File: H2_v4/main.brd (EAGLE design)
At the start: 160 x 100 mm, 15 parts, among them Q3 SOT-23, Q4 SOT-23, Q5 SOT-23, Q6 SOT-23

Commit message: Daily updates. Schematic done, board mostly done
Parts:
- removed Q1, Q2: (no value), Custom_old (1):POWERDI3333-8
- added C1, C11, C2, C3, C5: 0.1uF, SparkFun-Passives:0603-CAP
- added C10, C12, C4, C6, C7, C8, C9: 10uF, SparkFun-Passives:1206
- added D3: (no value), SparkFun-DiscreteSemi:SOD-123
- added IC1: (no value), 2018:V78W
- added LED1, LED2: (no value), SparkFun-LED:LED-1206
- added Q7, Q8: MOSFET-NCHANNELDFN5X6, 2018:DFN5X6
- added R1, R16, R17, R2: 1k, SparkFun-Passives:0603-RES
- added R10, R11, R12, R13, R14, R9: 4.7k, SparkFun-Passives:0603-RES
- added R15, R7: 10k, SparkFun-Passives:0603-RES
- added R3, R6: open, SparkFun-Passives:0603-RES
- added R4: 200m, SparkFun-Passives:0603-RES
- added R5: 0, SparkFun-Passives:0603-RES
- added R8: 1.2k, SparkFun-Passives:0603-RES
- added U$10, U$11: PAD, Custom_old (1):PAD
- added U$12: (no value), 2018:CAP-RADIAL
- added U$13: HEADER2, Custom_old:2PINVALULOK
- added U$14, U$15, U$18, U$19: SCREW, Custom_old:M3HOLE
- added U$16, U$17: (no value), 2018:DO-214AB
- added U$20, U$9: HEADER4VALULOK, Custom_old:4PINVALULOK
- added U$8: TEENSY_3.0_BASIC, Teensy3.0:TEENSY_3.0_BASIC
- U$1: value PRO-MINI-2 -> SHUNT_KELVIN; device Arduino-clone:PRO-MINI-2 -> 2018:2512_KELVIN
- U$5: value PAD -> HEADER8; device Custom_old (1):PAD -> Custom_old:8PINVALULOK
- U$6: value PAD -> LTC7001; device Custom_old (1):PAD -> 2018:PSOP-10
- moved Q6 126.0 mm to (41.0, 58.0)
- moved Q5 124.9 mm to (49.0, 58.0)
- moved D1 120.6 mm to (36.0, 65.0), turned to 180 degrees
- moved D2 119.6 mm to (31.0, 65.0), turned to 180 degrees
- moved Q3 73.5 mm to (45.0, 58.0)
- moved U$5 72.9 mm to (23.0, 70.0)
- moved U$2 65.4 mm to (17.9, 26.7), turned to 270 degrees
- moved Q4 53.6 mm to (21.0, 57.0)
- moved U$7 53.1 mm to (47.0, 48.0)
- moved U$6 51.6 mm to (26.0, 18.0)
- moved U$4 49.1 mm to (6.00, 4.00)
- moved U$1 36.4 mm to (14.0, 9.00)
- moved U$3 36.0 mm to (6.00, 11.0)
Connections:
- removed net 12V: D1.C, D2.C, U$5.PAD, U$7.POS
- removed net BUZZER: Q5.1
- removed net N$4: Q6.3
- removed net PASS_GATE: Q2.G
- removed net SC_GATE: Q1.G
- new net 5V: C3.2, C8.1, C9.1, IC1.OUT, R5.2, U$6.1, U$8.VIN
- new net ACC: C10.1, C4.1, D1.C, D2.C, R6.2, U$20.1, U$5.6, U$5.8, U$7.POS
- new net BUTTON: R15.1, U$13.2, U$8.16/A2
- new net BUZZ_G: Q5.1, U$8.9
- new net CAP_OUT: C5.2, Q8.1, Q8.2, Q8.3, U$10.PAD, U$12.+, U$17.C, U$6.8
- new net FAN_H: D3.C, R3.1, R5.1, R6.1, U$5.4
- new net FAN_L: D3.A, Q6.3, U$5.3
- new net FAN_SENSE: C2.1, R7.2, U$8.14/A0
- new net FC_POS: C6.1, C7.1, IC1.IN, Q7.PAD, Q8.PAD, R3.2, U$1.I+
- new net FC_RAW: C12.1, U$1.I-, U$16.C, U$3.PAD
- new net LED1: R16.1, U$8.10
- new net LED2: R17.1, U$8.11
- new net N$10: R10.2, U$9.2
- new net N$11: LED2.A, R17.2
- new net N$7: R1.1, U$1.V-
- new net N$8: R2.1, U$1.V+
- new net N$9: Q6.2, R4.2, R7.1
- new net PASS_CTRL: U$6.4, U$8.7
- new net PASS_G: Q8.4, U$6.6, U$6.7
- new net RX_FLOW: R10.1, R9.1, U$8.0
- new net SCL_EXT: R12.2, U$20.4, U$8.22/A8
- new net SC_G: Q7.4, U$8.8
- new net SDA_EXT: R11.2, U$20.3, U$8.23/A9
- new net THERM: R8.2, U$5.2, U$8.15/A1
- new net TX_FLOW: U$8.1, U$9.3
- new net VBAT: U$8.VBAT
- net 3.3V: now also C11.1, R11.1, R12.1, R13.1, R14.1, R15.2, R8.1, U$8.3.3V, U$8.3.3V1
- net FAN_G: now also U$8.4
- net GND: now also C10.2, C11.2, C12.2, C2.2, C3.1, C4.2, C6.2, C7.2, C8.2, C9.2, IC1.GND, LED1.C, LED2.C, Q7.1, Q7.2, Q7.3, R4.1, R9.2, U$11.PAD, U$12.-, U$13.1, U$16.A, U$17.A, U$20.2, U$4.PAD, U$5.1, U$6.2, U$6.3, U$6.5, U$8.AGND, U$8.GND, U$8.GND1, U$9.1; no longer Q6.2, U$6.PAD
- net N$1: now also C5.1, U$6.9; no longer Q1.D1, Q1.D2, Q1.D3, Q1.D4, Q1.D5, Q2.D1, Q2.D2, Q2.D3, Q2.D4, Q2.D5, U$3.PAD
- net N$2: now also LED1.A, R16.2; no longer Q1.S1, Q1.S2, Q1.S3, U$4.PAD
- net PRG-: now also U$5.5
- net PRG_G: now also U$8.6
- net SCL: now also R13.2, U$8.19/A5
- net SDA: now also R14.2, U$8.18/A4
- net SHUNT+: now also C1.1, R1.2
- net SHUNT-: now also C1.2, R2.2
- net SV-: now also U$5.7
- net SV_G: now also U$8.5
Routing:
- net 3.3V: track 0.00 -> 41.7 mm
- net CAP_OUT: track 0.00 -> 38.0 mm
- net GND: track 0.00 -> 27.9 mm, vias 0 -> 20
- net N$10: track 0.00 -> 19.6 mm
- net FC_RAW: track 0.00 -> 19.4 mm
- net SCL_EXT: track 0.00 -> 17.9 mm
- net SDA_EXT: track 0.00 -> 14.8 mm
- net SHUNT+: track 0.00 -> 12.6 mm
- net N$7: track 0.00 -> 10.5 mm
- net FC_POS: track 0.00 -> 9.37 mm
- net PASS_G: track 0.00 -> 8.75 mm
- net 5V: track 0.00 -> 8.55 mm
- net SHUNT-: track 0.00 -> 6.93 mm
- net N$1: track 0.00 -> 5.77 mm
- net N$8: track 0.00 -> 4.96 mm
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- added copper zone on layer 1, net CAP_OUT
- added copper zone on layer 1, net FC_POS
- added copper zone on layer 1, net FC_RAW
- added copper zone on layer 1, net GND
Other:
- board size 160 x 100 mm -> 54 x 78 mm
- board text added: "BTN"
- board text added: "FLOW"
- board text added: "IN"
- board text added: "OUT"

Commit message: First rev of h2v4 finished
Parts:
- moved C3 51.0 mm to (27.0, 22.0), turned to 180 degrees
- moved Q4 20.0 mm to (41.0, 58.0)
- moved Q6 18.0 mm to (23.0, 57.0)
- moved R8 17.5 mm to (14.0, 65.0), turned to 0 degrees
- moved R15 17.0 mm to (28.0, 58.0), turned to 270 degrees
- moved R6 5.00 mm to (15.0, 58.0)
- moved R3 3.00 mm to (17.0, 58.0)
- moved R5 1.00 mm to (13.0, 58.0)
- turned U$7 to 270 degrees
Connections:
- net CAP_OUT: now also C6.1, C7.1, IC1.IN, R3.2
- net FAN_SENSE: now also U$8.17/A3; no longer U$8.14/A0
- net FC_POS: no longer C6.1, C7.1, IC1.IN, R3.2
- net PASS_CTRL: now also U$8.3; no longer U$8.7
- net THERM: now also U$8.21/A7; no longer U$8.15/A1
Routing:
- net ACC: track 0.00 -> 138.0 mm, vias 0 -> 3
- net CAP_OUT: track 38.0 -> 102.3 mm, vias 0 -> 2
- net 5V: track 8.55 -> 69.5 mm, vias 0 -> 3
- net SC_G: track 0.00 -> 58.7 mm, vias 0 -> 2
- net 3.3V: track 41.7 -> 98.6 mm, vias 0 -> 3
- net SCL: track 0.00 -> 56.1 mm, vias 0 -> 4
- net SDA: track 0.00 -> 55.0 mm, vias 0 -> 2
- net TX_FLOW: track 0.00 -> 41.6 mm, vias 0 -> 1
- net PASS_CTRL: track 0.00 -> 37.0 mm
- net SV_G: track 0.00 -> 31.2 mm, vias 0 -> 2
- net SCL_EXT: track 17.9 -> 49.0 mm, vias 0 -> 2
- net PRG-: track 0.00 -> 27.0 mm
- net FAN_H: track 0.00 -> 27.0 mm, vias 0 -> 1
- net SV-: track 0.00 -> 25.2 mm
- net PRG_G: track 0.00 -> 25.1 mm
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- added copper zone on layer 16, net GND
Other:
- board text added: "+"
- board text added: "ACC"
- board text added: "BMS"
- board text added: "BTN+"
- board text added: "FAN_H"
- board text added: "FAN_L"
- board text added: "FLOW TX TEENS RX"
- board text added: "FLOW_RX TEENS_TX"
- board text added: "GND"
- board text added: "IN-"
- board text added: "OUT-"
- board text added: "PRG-"
- board text added: "SCL"
- board text added: "SDA"
- board text added: "SV-"
- board text added: "THERM"
- board text removed: "IN"
- board text removed: "OUT"

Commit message: Final
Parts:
- U$6: device 2018:PSOP-10 -> 2018:PSOP-10-EP
- moved U$6 2.30 mm to (28.3, 18.0)
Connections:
- net GND: now also U$6.PAD
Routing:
- net CAP_OUT: track 102.3 -> 105.4 mm
- net GND: vias 26 -> 80
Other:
- board text added: "5v ACC FC"
- board text added: "FUEL CELL"
- board text added: "H2 Controller v4 Designed by PLG 06/2018"
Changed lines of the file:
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@@
 <layer number="23" name="tOrigins" color="15" fill="1" visible="yes" active="yes"/>
 <layer number="24" name="bOrigins" color="15" fill="1" visible="yes" active="yes"/>
-<layer number="25" name="tNames" color="7" fill="1" visible="yes" active="yes"/>
-<layer number="26" name="bNames" color="7" fill="1" visible="yes" active="yes"/>
-<layer number="27" name="tValues" color="7" fill="1" visible="yes" active="yes"/>
-<layer number="28" name="bValues" color="7" fill="1" visible="yes" active="yes"/>
+<layer number="25" name="tNames" color="7" fill="1" visible="no" active="yes"/>
+<layer number="26" name="bNames" color="7" fill="1" visible="no" active="yes"/>
+<layer number="27" name="tValues" color="7" fill="1" visible="no" active="yes"/>
+<layer number="28" name="bValues" color="7" fill="1" visible="no" active="yes"/>
 <layer number="29" name="tStop" color="7" fill="3" visible="yes" active="yes"/>
 <layer number="30" name="bStop" color="7" fill="6" visible="yes" active="yes"/>
@@
 <wire x1="54" y1="78" x2="0" y2="78" width="0" layer="20"/>
 <wire x1="0" y1="78" x2="0" y2="0" width="0" layer="20"/>
-<text x="7" y="66" size="1.4224" layer="21">FLOW</text>
-<text x="48" y="70" size="1.4224" layer="21" rot="R90">BTN</text>
+<text x="10" y="66" size="1.4224" layer="21">FLOW</text>
+<text x="41" y="66" size="1.4224" layer="21">BTN</text>
 <text x="12" y="3" size="2.54" layer="21">IN-</text>
 <text x="34" y="3" size="2.54" layer="21">OUT-</text>
@@
 <text x="13.6" y="9.6" size="2.54" layer="21" rot="MR0">+</text>
 <text x="40" y="10" size="2.54" layer="21">+</text>
+<text x="41" y="44" size="1.27" layer="22" rot="MR270">H2 Controller v4
+Designed by PLG 06/2018</text>
+<text x="25" y="66" size="1.27" layer="21">FUEL CELL</text>
+<text x="17.5" y="52.1" size="1.27" layer="21" rot="R90">5v
+ACC
+FC</text>
 </plain>
 <attributes>
@@
 <element name="R13" library="SparkFun-Passives" package="0603-RES" value="4.7k" x="4" y="55"/>
 <element name="R14" library="SparkFun-Passives" package="0603-RES" value="4.7k" x="4" y="53"/>
-<element name="U$6" library="2018" package="PSOP-10" value="LTC7001" x="26" y="18"/>
+<element name="U$6" library="2018" package="PSOP-10-EP" value="LTC7001" x="28.3" y="18"/>
 <element name="U$10" library="Custom_old (1)" package="PAD" value="PAD" x="48" y="11"/>
 <element name="U$11" library="Custom_old (1)" package="PAD" value="PAD" x="48" y="4"/>
@@
 <contactref element="U$6" pad="7"/>
 <contactref element="Q8" pad="4"/>
-<wire x1="30.5" y1="17.5" x2="30.5" y2="17" width="0.1524" layer="1"/>
-<wire x1="30.5" y1="17" x2="32.5" y2="15" width="0.2032" layer="1"/>
+<wire x1="30.514" y1="17.5" x2="30.514" y2="17" width="0.1524" layer="1"/>
+<wire x1="30.514" y1="17" x2="32.5" y2="15" width="0.2032" layer="1"/>
 <wire x1="32.5" y1="15" x2="35" y2="15" width="0.2032" layer="1"/>
 <wire x1="35" y1="15" x2="37" y2="13" width="0.2032" layer="1"/>
@@
 <wire x1="2" y1="25" x2="3" y2="26" width="0.2032" layer="1"/>
 <wire x1="3" y1="26" x2="3" y2="33" width="0.2032" layer="1"/>
-<wire x1="26" y1="18" x2="26" y2="18.5" width="0.2032" layer="1"/>
+<wire x1="26.014" y1="18" x2="26.014" y2="18.5" width="0.2032" layer="1"/>
 <wire x1="18.81" y1="35" x2="23.4" y2="35" width="0.8128" layer="1"/>
 <wire x1="23.4" y1="35" x2="24" y2="35.6" width="0.8128" layer="1"/>
@@
 <via x="38" y="18" extent="1-16" drill="0.4"/>
 <via x="38" y="16" extent="1-16" drill="0.4"/>
+<contactref element="U$6" pad="PAD"/>
+<via x="18" y="4" extent="1-16" drill="0.4"/>
+<via x="22" y="4" extent="1-16" drill="0.4"/>
+<via x="26" y="4" extent="1-16" drill="0.4"/>
+<via x="30" y="4" extent="1-16" drill="0.4"/>
+<via x="34" y="4" extent="1-16" drill="0.4"/>
+<via x="2" y="28" extent="1-16" drill="0.4"/>
+<via x="2" y="21" extent="1-16" drill="0.4"/>
+<via x="7" y="21" extent="1-16" drill="0.4"/>
+<via x="7" y="15" extent="1-16" drill="0.4"/>
+<via x="14" y="15" extent="1-16" drill="0.4"/>
+<via x="19" y="14" extent="1-16" drill="0.4"/>
+<via x="27.6" y="20" extent="1-16" drill="0.4"/>
+<via x="29" y="20" extent="1-16" drill="0.4"/>
+<via x="27.7" y="16" extent="1-16" drill="0.4"/>
+<via x="29" y="16" extent="1-16" drill="0.4"/>
+<via x="25" y="20" extent="1-16" drill="0.4"/>
+<via x="42" y="35" extent="1-16" drill="0.4"/>
+<via x="42" y="33" extent="1-16" drill="0.4"/>
+<via x="49" y="33" extent="1-16" drill="0.4"/>
+<via x="49" y="35" extent="1-16" drill="0.4"/>
+<via x="31" y="32" extent="1-16" drill="0.4"/>
+<via x="34" y="32" extent="1-16" drill="0.4"/>
+<via x="27" y="34" extent="1-16" drill="0.4"/>
+<via x="25" y="34" extent="1-16" drill="0.4"/>
+<via x="23" y="34" extent="1-16" drill="0.4"/>
+<via x="21" y="34" extent="1-16" drill="0.4"/>
+<via x="24" y="27" extent="1-16" drill="0.4"/>
+<via x="20" y="26" extent="1-16" drill="0.4"/>
+<via x="20" y="24" extent="1-16" drill="0.4"/>
+<via x="15" y="26" extent="1-16" drill="0.4"/>
+<via x="15" y="24" extent="1-16" drill="0.4"/>
+<via x="22" y="42" extent="1-16" drill="0.4"/>
+<via x="14" y="36" extent="1-16" drill="0.4"/>
+<via x="44" y="55" extent="1-16" drill="0.4"/>
+<via x="48" y="55" extent="1-16" drill="0.4"/>
+<via x="47" y="60" extent="1-16" drill="0.4"/>
+<via x="43" y="60" extent="1-16" drill="0.4"/>
+<via x="48" y="67" extent="1-16" drill="0.4"/>
+<via x="51" y="67" extent="1-16" drill="0.4"/>
+<via x="51" y="69" extent="1-16" drill="0.4"/>
+<via x="48" y="69" extent="1-16" drill="0.4"/>
+<via x="39" y="68" extent="1-16" drill="0.4"/>
+<via x="20.5" y="70.5" extent="1-16" drill="0.4"/>
+<via x="18" y="70" extent="1-16" drill="0.4"/>
+<via x="4" y="70" extent="1-16" drill="0.4"/>
+<via x="8" y="64" extent="1-16" drill="0.4"/>
+<via x="6" y="64" extent="1-16" drill="0.4"/>
+<via x="47" y="16" extent="1-16" drill="0.4"/>
+<via x="12.4" y="49.7" extent="1-16" drill="0.4"/>
+<via x="31.6" y="60" extent="1-16" drill="0.4"/>
+<via x="23" y="65" extent="1-16" drill="0.4"/>
+<via x="8" y="56" extent="1-16" drill="0.4"/>
+<via x="10" y="39" extent="1-16" drill="0.4"/>
+<via x="27" y="51" extent="1-16" drill="0.4"/>
 </signal>
 <signal name="3.3V">
@@
 <wire x1="23.14" y1="37.54" x2="24" y2="38.4" width="0.8128" layer="1"/>
 <wire x1="24" y1="38.4" x2="27" y2="38.4" width="0.8128" layer="1"/>
-<wire x1="26" y1="19" x2="26" y2="22" width="0.2032" layer="1"/>
+<wire x1="26.014" y1="19" x2="26" y2="22" width="0.2032" layer="1"/>
 <wire x1="26" y1="22" x2="26" y2="23" width="0.2032" layer="1"/>
 <wire x1="26" y1="23" x2="19" y2="30" width="0.2032" layer="1"/>
@@
 <contactref element="R3" pad="2"/>
 <wire x1="27" y1="29.6" x2="27.3" y2="29.3" width="0.508" layer="1"/>
-<wire x1="27.3" y1="29.3" x2="34.3" y2="22.3" width="0.508" layer="1"/>
 <wire x1="34.3" y1="22.3" x2="36" y2="20.6" width="0.508" layer="1"/>
 <wire x1="36" y1="20.6" x2="36" y2="18" width="0.508" layer="1"/>
@@
 <wire x1="31.85" y1="22" x2="32.15" y2="22.3" width="0.254" layer="1"/>
 <wire x1="32.15" y1="22.3" x2="34.3" y2="22.3" width="0.254" layer="1"/>
-<wire x1="30.5" y1="18" x2="36" y2="18" width="0.254" layer="1"/>
+<wire x1="30.514" y1="18" x2="36" y2="18" width="0.254" layer="1"/>
 <wire x1="17" y1="57.15" x2="16.9" y2="57.05" width="0.2032" layer="1"/>
 <wire x1="16.9" y1="57.05" x2="16.9" y2="56.5" width="0.2032" layer="1"/>
@@
 <wire x1="27.3" y1="29.6" x2="27.3" y2="29.3" width="0.2032" layer="1"/>
 <wire x1="26.2" y1="44.2" x2="28.4" y2="42" width="0.2032" layer="1"/>
+<wire x1="34.3" y1="22.3" x2="32.6" y2="24" width="0.508" layer="1"/>
+<wire x1="32.6" y1="24" x2="28" y2="24" width="0.508" layer="1"/>
+<wire x1="28" y1="24" x2="27" y2="25" width="0.508" layer="1"/>
+<wire x1="27" y1="25" x2="27" y2="29.6" width="0.508" layer="1"/>
 </signal>
 <signal name="N$1">
 <contactref element="U$6" pad="9"/>
 <contactref element="C5" pad="1"/>
-<wire x1="30.5" y1="18.5" x2="32" y2="18.5" width="0.2032" layer="1"/>
+<wire x1="30.514" y1="18.5" x2="32" y2="18.5" width="0.2032" layer="1"/>
 <wire x1="32" y1="18.5" x2="32" y2="20" width="0.2032" layer="1"/>
 <wire x1="32" y1="20" x2="30.15" y2="21.85" width="0.2032" layer="1"/>
@@
 <contactref element="U$6" pad="4"/>
 <contactref element="U$8" pad="3"/>
-<wire x1="26" y1="17.5" x2="24.5" y2="17.5" width="0.2032" layer="1"/>
+<wire x1="26.014" y1="17.5" x2="24.5" y2="17.5" width="0.2032" layer="1"/>
 <wire x1="24.5" y1="17.5" x2="24" y2="18" width="0.2032" layer="1"/>
 <wire x1="18.7" y1="29.3" x2="17.7" y2="29.3" width="0.2032" layer="1"/>

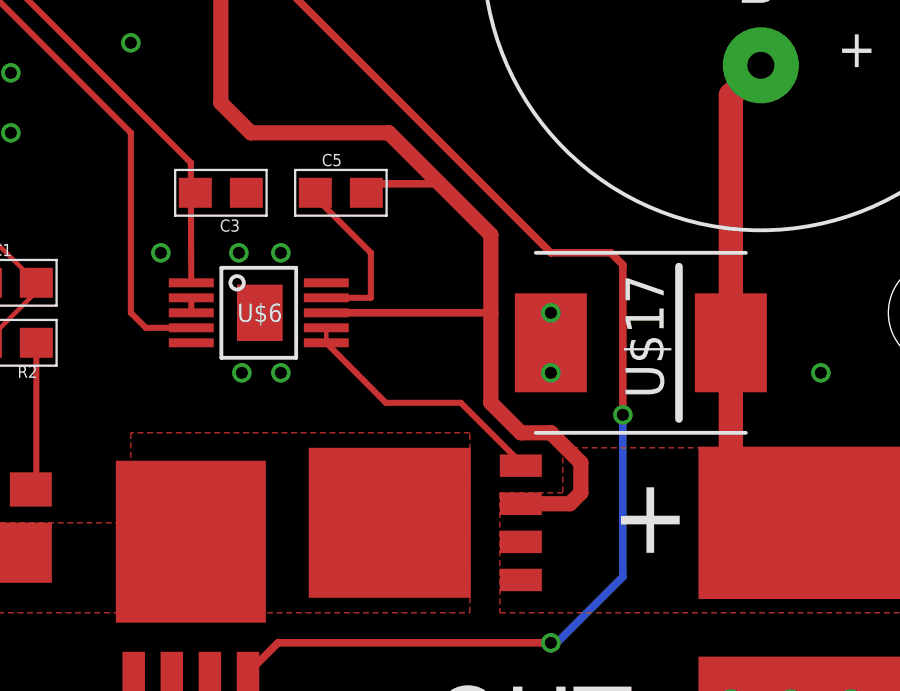
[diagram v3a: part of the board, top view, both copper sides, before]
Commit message: fixed pass mosfet
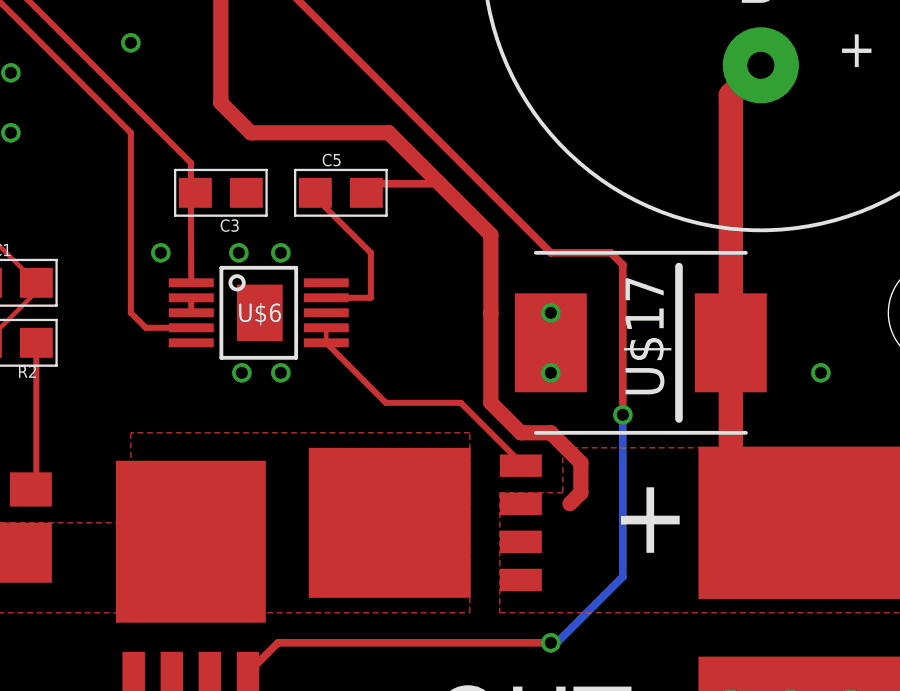
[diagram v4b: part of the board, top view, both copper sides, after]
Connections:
- net CAP_OUT: now also Q8.PAD; no longer C5.2, Q8.1, Q8.2, Q8.3, U$6.8
- net FC_POS: now also C5.2, Q8.1, Q8.2, Q8.3, U$6.8; no longer Q8.PAD
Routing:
- net CAP_OUT: track 105.4 -> 97.9 mm
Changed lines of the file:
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@@
 <?xml version="1.0" encoding="utf-8"?>
 <!DOCTYPE eagle SYSTEM "eagle.dtd">
-<eagle version="8.7.1">
+<eagle version="9.1.1">
 <drawing>
 <settings>
@@
 <param name="checkStop" value="0"/>
 <param name="checkValues" value="0"/>
+<param name="checkNames" value="1"/>
+<param name="checkWireStubs" value="1"/>
+<param name="checkPolygonWidth" value="0"/>
 <param name="useDiameter" value="13"/>
 <param name="maxErrors" value="50"/>
@@
 <signal name="FC_POS">
 <contactref element="U$1" pad="I+"/>
-<contactref element="Q8" pad="PAD"/>
 <contactref element="Q7" pad="PAD"/>
 <polygon width="0.2032" layer="1" thermals="no">
@@
 <vertex x="24" y="11"/>
 </polygon>
+<contactref element="Q8" pad="2"/>
+<contactref element="Q8" pad="3"/>
+<contactref element="Q8" pad="1"/>
+<contactref element="U$6" pad="8"/>
+<contactref element="C5" pad="2"/>
+<wire x1="30.514" y1="18" x2="31.85" y2="22" width="0" layer="19" extent="1-1"/>
+<wire x1="26" y1="10.37" x2="30.514" y2="18" width="0" layer="19" extent="1-1"/>
+<wire x1="19.842" y1="10.0033" x2="26" y2="10.37" width="0" layer="19" extent="1-1"/>
+<wire x1="37" y1="11.635" x2="30.514" y2="18" width="0" layer="19" extent="1-1"/>
+<wire x1="37" y1="10.365" x2="37" y2="11.635" width="0" layer="19" extent="1-1"/>
+<wire x1="37" y1="9.095" x2="37" y2="10.365" width="0" layer="19" extent="1-1"/>
 </signal>
 <signal name="PASS_G">
@@
 <signal name="CAP_OUT">
 <contactref element="U$10" pad="PAD"/>
-<contactref element="U$6" pad="8"/>
-<contactref element="C5" pad="2"/>
 <contactref element="U$12" pad="+"/>
 <contactref element="U$17" pad="C"/>
-<contactref element="Q8" pad="3"/>
-<contactref element="Q8" pad="1"/>
-<contactref element="Q8" pad="2"/>
 <polygon width="0.2032" layer="1" thermals="no">
 <vertex x="36.3" y="12"/>
@@
 <wire x1="39" y1="13" x2="39" y2="12" width="0.508" layer="1"/>
 <wire x1="39" y1="12" x2="38.635" y2="11.635" width="0.508" layer="1"/>
-<wire x1="38.635" y1="11.635" x2="37" y2="11.635" width="0.508" layer="1"/>
-<wire x1="31.85" y1="22" x2="32.15" y2="22.3" width="0.254" layer="1"/>
 <wire x1="32.15" y1="22.3" x2="34.3" y2="22.3" width="0.254" layer="1"/>
-<wire x1="30.514" y1="18" x2="36" y2="18" width="0.254" layer="1"/>
 <wire x1="17" y1="57.15" x2="16.9" y2="57.05" width="0.2032" layer="1"/>
 <wire x1="16.9" y1="57.05" x2="16.9" y2="56.5" width="0.2032" layer="1"/>
@@
 <wire x1="28" y1="24" x2="27" y2="25" width="0.508" layer="1"/>
 <wire x1="27" y1="25" x2="27" y2="29.6" width="0.508" layer="1"/>
+<contactref element="Q8" pad="PAD"/>
+<wire x1="39" y1="12" x2="44" y2="11" width="0" layer="19" extent="1-1"/>
+<wire x1="32.63" y1="11" x2="36" y2="15" width="0" layer="19" extent="1-1"/>
 </signal>
 <signal name="N$1">
@@
 </signal>
 </signals>
+<mfgpreviewcolors>
+<mfgpreviewcolor name="soldermaskcolor" color="0xC8008000"/>
+<mfgpreviewcolor name="silkscreencolor" color="0xFFFEFEFE"/>
+<mfgpreviewcolor name="backgroundcolor" color="0xFF282828"/>
+<mfgpreviewcolor name="coppercolor" color="0xFFFFBF00"/>
+<mfgpreviewcolor name="substratecolor" color="0xFF786E46"/>
+</mfgpreviewcolors>
 </board>
 </drawing>
